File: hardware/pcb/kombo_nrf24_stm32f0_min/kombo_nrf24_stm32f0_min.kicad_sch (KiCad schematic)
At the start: 18 parts, among them J1 Conn_01x02, J2 Conn_01x04, J3 Conn_01x04, J4 Conn_01x04, U1 NRF24L01_Breakout, U2 AMS1117-3.3, U3 STM32F030F4Px

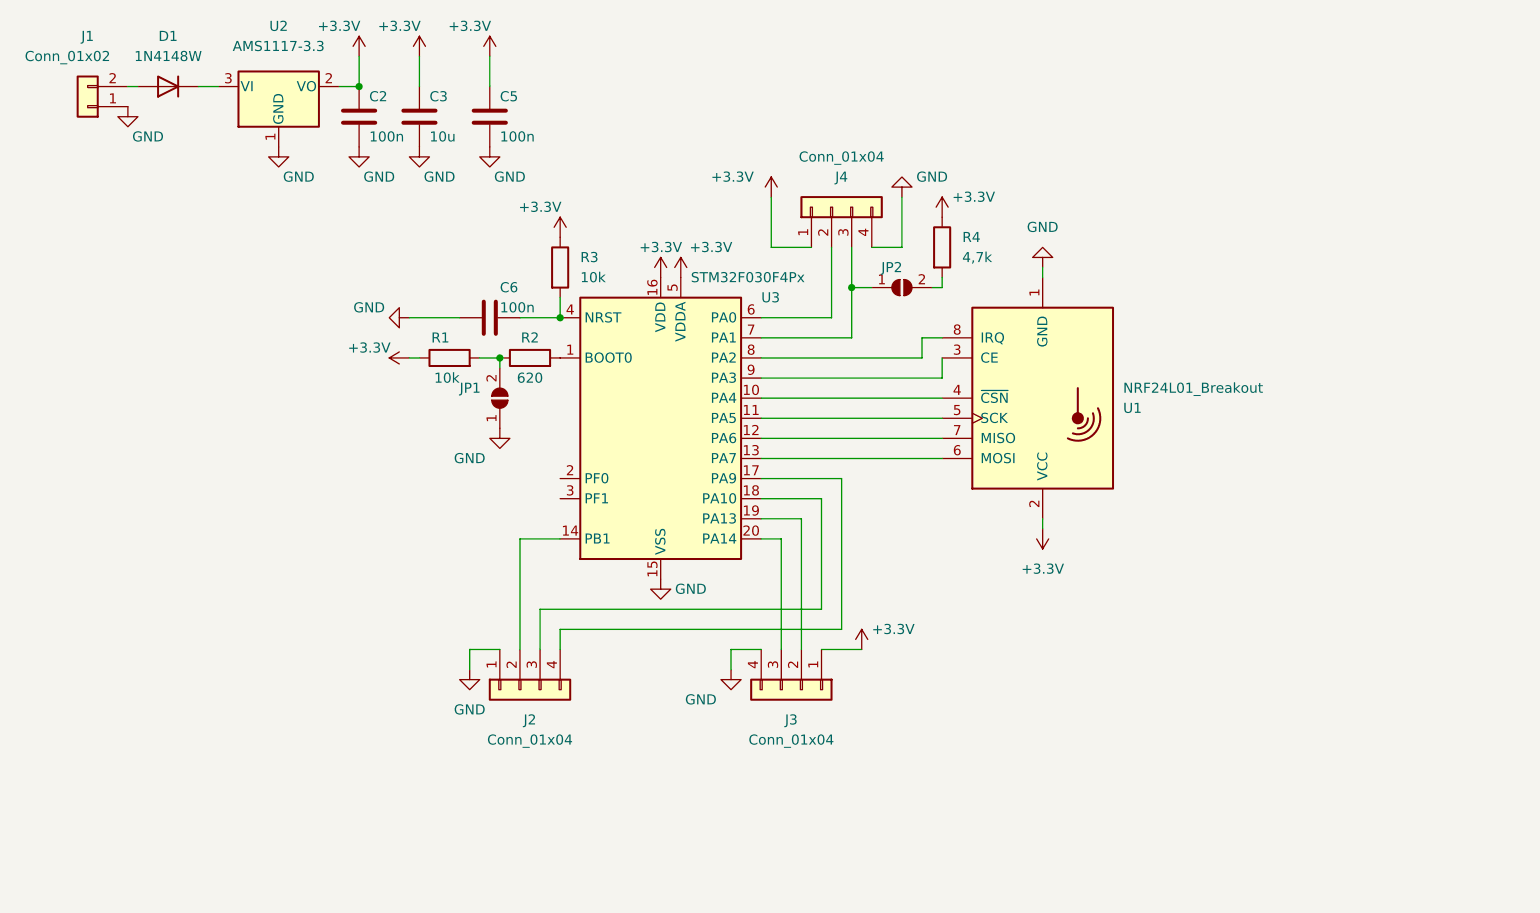
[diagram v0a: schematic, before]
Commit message: 15/01/2024
✅ - обновлена библиотека работы с модулем nrf24l01+
✅ - добавлена библиотека работы с адресными светодиодами ws2812
✅ - обновлены файлы печатных плат
✅ - добавлены файлы печатных плат микроконтроллера stm32f030f4p6 c nrf24l01+
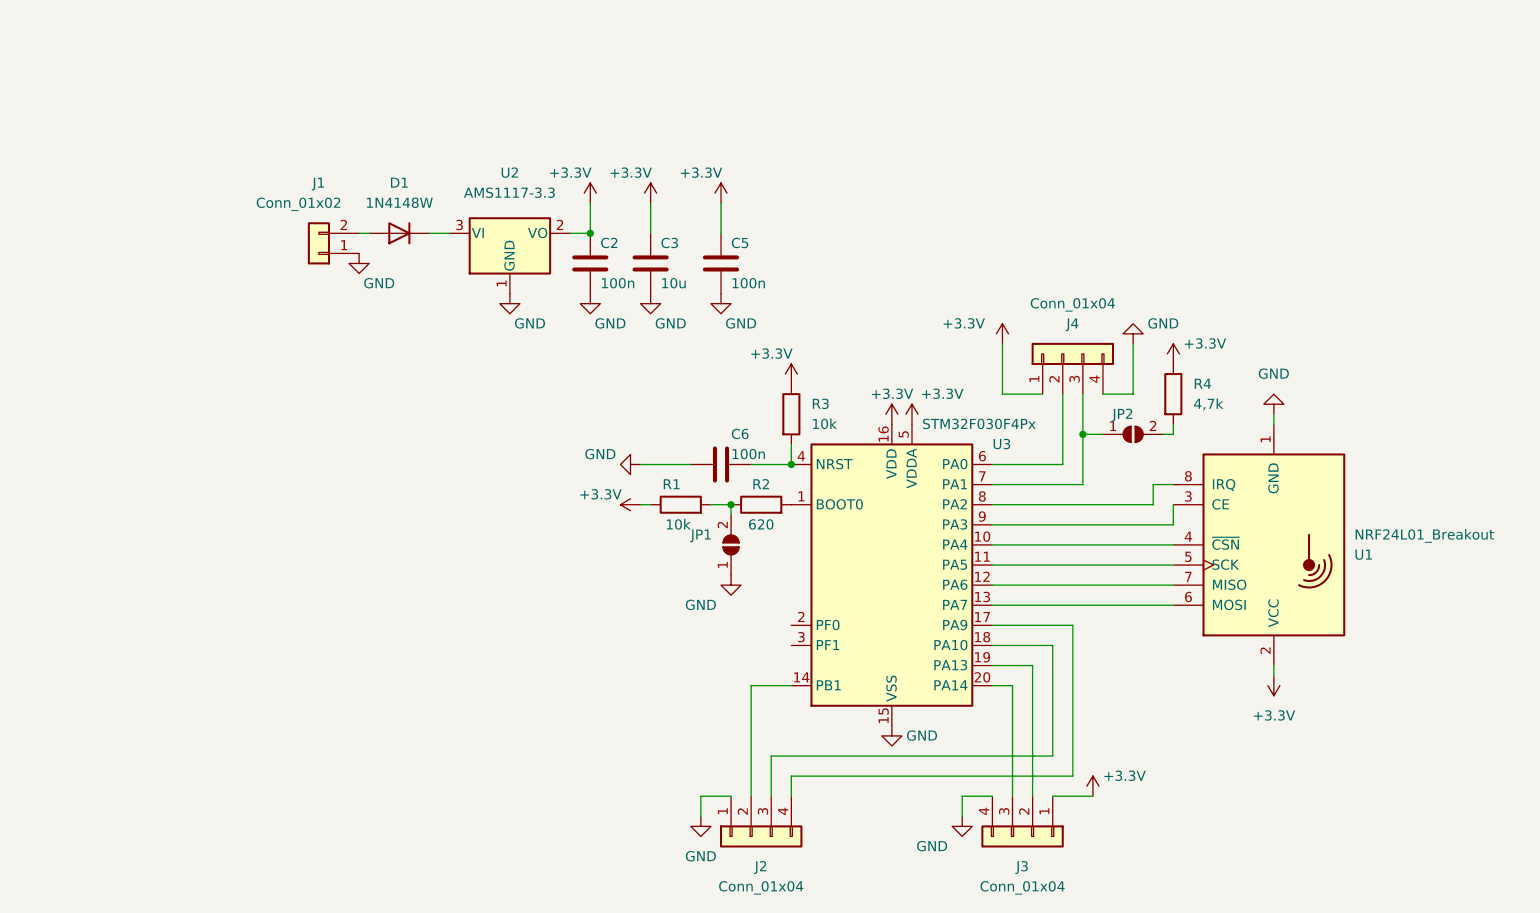
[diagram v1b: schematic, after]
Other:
- moved on the sheet: C2, C3, C5, C6, D1, J1, J2, J3, J4, JP1, JP2, R1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
